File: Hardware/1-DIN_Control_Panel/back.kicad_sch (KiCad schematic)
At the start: 49 parts, among them J1 Selector Knob Connector, J10 2x05 Molex Micro-Fit 3.0 43045, J13 Mode LEDs, J14 Selector Knob Connector, J15 Rotary Switch 1x7, J16 Mode LEDs, J2 Rotary Switch 1x7, J3 2x05 Molex Micro-Fit 3.0 43045, J4 UART Expansion, J5 SW - Aux Jump-Start, J6 SW - Battery Bypass, J7 SW - Master Power, J8 Pot/SW - Brightness, K1 FINDER-40.52, U12 LM324DR, U13 12V->5V Variable Boost Buck C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, U15 LTV-847S, U16 LTV-847S, U5 MMPQ3904, U6 MMPQ3904

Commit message: Fixed BJT math
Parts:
- removed J14: Selector Knob Connector, Connector_Molex:Molex_Micro-Fit_3.0_43045-0812_2x04_P3.00mm_Vertical, symbol Connector_Generic:Conn_01x08
- removed J15: Rotary Switch 1x7, Connector_Molex:Molex_Micro-Fit_3.0_43045-0812_2x04_P3.00mm_Vertical, symbol Connector_Generic:Conn_01x08
- removed J16: Mode LEDs, Connector_Molex:Molex_Micro-Fit_3.0_43045-0812_2x04_P3.00mm_Vertical, symbol Connector_Generic:Conn_01x08
- removed R21: 10kΩ, Resistor_SMD:R_0603_1608Metric_Pad0.98x0.95mm_HandSolder, symbol Device:R_US
- removed U15, U16: LTV-847S, Package_DIP:SMDIP-16_W9.53mm, symbol Isolator:LTV-847S
- added R22, R23, R24, R25, R26, R27, R28, R29: 39kΩ, Resistor_SMD:R_0603_1608Metric_Pad0.98x0.95mm_HandSolder, symbol Device:R_US
- renumbered J1 to J14, J2 to J15, J13 to J16, U5 to U15, U6 to U16
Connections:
- net GND: no longer U16.10 (E4)
- net MODE_1: now also R22.2; no longer U15.15 (B1)
- net MODE_12V: now also R29.2; no longer U16.9 (B4)
- net MODE_2: now also R23.2; no longer U15.13 (B2)
- net MODE_3: now also R24.2; no longer U15.11 (B3)
- net MODE_4: now also R25.2; no longer U15.9 (B4)
- net MODE_5: now also R26.2; no longer U16.15 (B1)
- net MODE_6: now also R27.2; no longer U16.13 (B2)
- net MODE_7: now also R28.2; no longer U16.11 (B3)
- net MODE_PWR_DETECT: now also U16.10 (E4)
- net at J16.8 (Pin_8): now also R9.2
- new net: R27.1, U16.13 (B2)
- new net: R24.1, U15.11 (B3)
- new net: R23.1, U15.13 (B2)
- new net: R26.1, U16.15 (B1)
- new net: R25.1, U15.9 (B4)
- new net: R22.1, U15.15 (B1)
- new net: R28.1, U16.11 (B3)
- new net: R29.1, U16.9 (B4)
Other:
- note added: "Using extra BJT as mode selector 12V detect signal...because why not!"
- note added: "Vbe = 0.7V 12V-ib(39kΩ)-Vbe = 0 -> ib = 0.290mA ic = hFE*ib = 70*0.290mA = 20mA"
- note removed: "Using extra optoisolator as mode selector 12V detect signal...because why not!"
- moved on the sheet: J14, J15, J16, U15A, U15B, U15C, U15D, U16A, U16B, U16C, U16D

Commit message: Almost done with routing
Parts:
- renumbered J14 to J1, J16 to J13, J15 to J2, U15 to U5, U16 to U6
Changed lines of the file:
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@@
   (symbol (lib_id "Panel_Parts:MMPQ3904") (at 102.87 152.4 0) (unit 2)
     (in_bom yes) (on_board yes) (dnp no)
-    (property "Reference" "U16" (at 106.68 151.13 0)
+    (property "Reference" "U6" (at 106.68 151.13 0)
       (effects (font (size 1.27 1.27)) (justify left))
     )
@@
       (project "1-DIN_Control_Panel"
         (path "/9d6c5460-8470-44bf-9076-df961456f999/79705e83-d37e-491a-a216-1b060693c97a"
-          (reference "U16") (unit 2)
+          (reference "U6") (unit 2)
         )
       )
@@
   (symbol (lib_id "Connector_Generic:Conn_01x08") (at 130.81 78.74 90) (unit 1)
     (in_bom yes) (on_board yes) (dnp no)
-    (property "Reference" "J16" (at 135.89 74.93 90)
+    (property "Reference" "J13" (at 135.89 74.93 90)
       (effects (font (size 1.27 1.27)) (justify right))
     )
@@
       (project "1-DIN_Control_Panel"
         (path "/9d6c5460-8470-44bf-9076-df961456f999/79705e83-d37e-491a-a216-1b060693c97a"
-          (reference "J16") (unit 1)
+          (reference "J13") (unit 1)
         )
       )
@@
   (symbol (lib_id "Connector_Generic:Conn_01x08") (at 62.23 74.93 270) (mirror x) (unit 1)
     (in_bom yes) (on_board yes) (dnp no)
-    (property "Reference" "J15" (at 73.66 72.39 90)
+    (property "Reference" "J2" (at 73.66 72.39 90)
       (effects (font (size 1.27 1.27)) (justify left))
     )
@@
       (project "1-DIN_Control_Panel"
         (path "/9d6c5460-8470-44bf-9076-df961456f999/79705e83-d37e-491a-a216-1b060693c97a"
-          (reference "J15") (unit 1)
+          (reference "J2") (unit 1)
         )
       )
@@
   (symbol (lib_id "Panel_Parts:MMPQ3904") (at 102.87 118.11 0) (unit 3)
     (in_bom yes) (on_board yes) (dnp no)
-    (property "Reference" "U15" (at 106.68 116.84 0)
+    (property "Reference" "U5" (at 106.68 116.84 0)
       (effects (font (size 1.27 1.27)) (justify left))
     )
@@
       (project "1-DIN_Control_Panel"
         (path "/9d6c5460-8470-44bf-9076-df961456f999/79705e83-d37e-491a-a216-1b060693c97a"
-          (reference "U15") (unit 3)
+          (reference "U5") (unit 3)
         )
       )
@@
   (symbol (lib_id "Connector_Generic:Conn_01x08") (at 30.48 105.41 180) (unit 1)
     (in_bom yes) (on_board yes) (dnp no)
-    (property "Reference" "J14" (at 38.862 105.7715 0)
+    (property "Reference" "J1" (at 25.4 104.14 0)
       (effects (font (size 1.27 1.27)) (justify right))
     )
@@
       (project "1-DIN_Control_Panel"
         (path "/9d6c5460-8470-44bf-9076-df961456f999/79705e83-d37e-491a-a216-1b060693c97a"
-          (reference "J14") (unit 1)
+          (reference "J1") (unit 1)
         )
       )
@@
   (symbol (lib_id "Panel_Parts:MMPQ3904") (at 102.87 129.54 0) (unit 4)
     (in_bom yes) (on_board yes) (dnp no)
-    (property "Reference" "U15" (at 106.68 128.27 0)
+    (property "Reference" "U5" (at 106.68 128.27 0)
       (effects (font (size 1.27 1.27)) (justify left))
     )
@@
       (project "1-DIN_Control_Panel"
         (path "/9d6c5460-8470-44bf-9076-df961456f999/79705e83-d37e-491a-a216-1b060693c97a"
-          (reference "U15") (unit 4)
+          (reference "U5") (unit 4)
         )
       )
@@
   (symbol (lib_id "Panel_Parts:MMPQ3904") (at 102.87 95.25 0) (unit 1)
     (in_bom yes) (on_board yes) (dnp no)
-    (property "Reference" "U15" (at 106.68 93.98 0)
+    (property "Reference" "U5" (at 106.68 93.98 0)
       (effects (font (size 1.27 1.27)) (justify left))
     )
@@
       (project "1-DIN_Control_Panel"
         (path "/9d6c5460-8470-44bf-9076-df961456f999/79705e83-d37e-491a-a216-1b060693c97a"
-          (reference "U15") (unit 1)
+          (reference "U5") (unit 1)
         )
       )
@@
   (symbol (lib_id "Panel_Parts:MMPQ3904") (at 102.87 163.83 0) (unit 3)
     (in_bom yes) (on_board yes) (dnp no)
-    (property "Reference" "U16" (at 106.68 162.56 0)
+    (property "Reference" "U6" (at 106.68 162.56 0)
       (effects (font (size 1.27 1.27)) (justify left))
     )
@@
       (project "1-DIN_Control_Panel"
         (path "/9d6c5460-8470-44bf-9076-df961456f999/79705e83-d37e-491a-a216-1b060693c97a"
-          (reference "U16") (unit 3)
+          (reference "U6") (unit 3)
         )
       )
@@
   (symbol (lib_id "Panel_Parts:MMPQ3904") (at 102.87 106.68 0) (unit 2)
     (in_bom yes) (on_board yes) (dnp no)
-    (property "Reference" "U15" (at 106.68 105.41 0)
+    (property "Reference" "U5" (at 106.68 105.41 0)
       (effects (font (size 1.27 1.27)) (justify left))
     )
@@
       (project "1-DIN_Control_Panel"
         (path "/9d6c5460-8470-44bf-9076-df961456f999/79705e83-d37e-491a-a216-1b060693c97a"
-          (reference "U15") (unit 2)
+          (reference "U5") (unit 2)
         )
       )
@@
   (symbol (lib_id "Panel_Parts:MMPQ3904") (at 102.87 140.97 0) (unit 1)
     (in_bom yes) (on_board yes) (dnp no)
-    (property "Reference" "U16" (at 106.68 139.7 0)
-      (effects (font (size 1.27 1.27)) (justify left))
-    )
-    (property "Value" "MMPQ3904" (at 87.63 158.75 0)
+    (property "Reference" "U6" (at 106.68 139.7 0)
+      (effects (font (size 1.27 1.27)) (justify left))
+    )
+    (property "Value" "MMPQ3904" (at 87.63 134.62 0)
       (effects (font (size 1.27 1.27)) (justify left))
     )
@@
       (project "1-DIN_Control_Panel"
         (path "/9d6c5460-8470-44bf-9076-df961456f999/79705e83-d37e-491a-a216-1b060693c97a"
-          (reference "U16") (unit 1)
+          (reference "U6") (unit 1)
         )
       )
@@
   (symbol (lib_id "Panel_Parts:MMPQ3904") (at 102.87 175.26 0) (unit 4)
     (in_bom yes) (on_board yes) (dnp no)
-    (property "Reference" "U16" (at 106.68 173.99 0)
+    (property "Reference" "U6" (at 106.68 173.99 0)
       (effects (font (size 1.27 1.27)) (justify left))
     )
@@
       (project "1-DIN_Control_Panel"
         (path "/9d6c5460-8470-44bf-9076-df961456f999/79705e83-d37e-491a-a216-1b060693c97a"
-          (reference "U16") (unit 4)
-        )
-      )
+          (reference "U6") (unit 4)
+        )
+      )

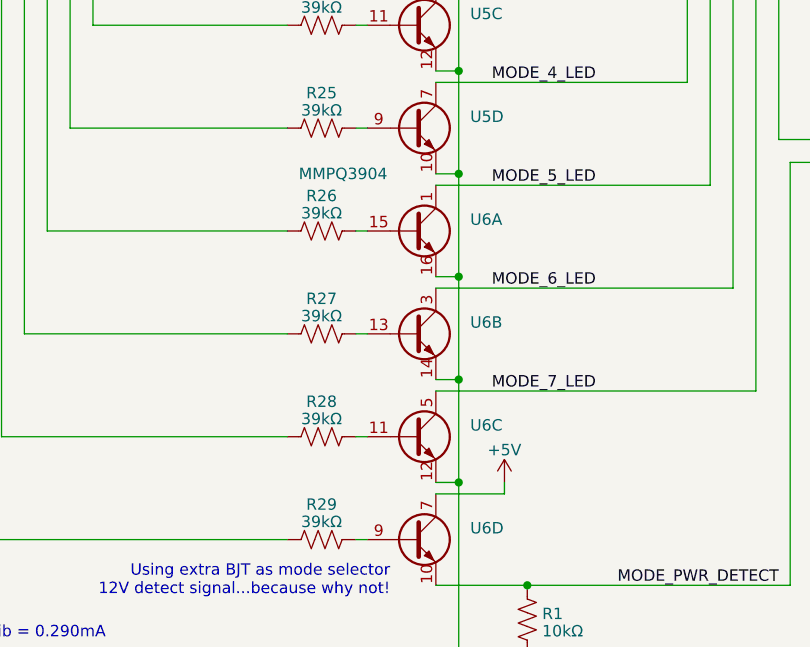
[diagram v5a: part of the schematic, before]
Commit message: Finished routing
Now just need to combine the boards with mousebites
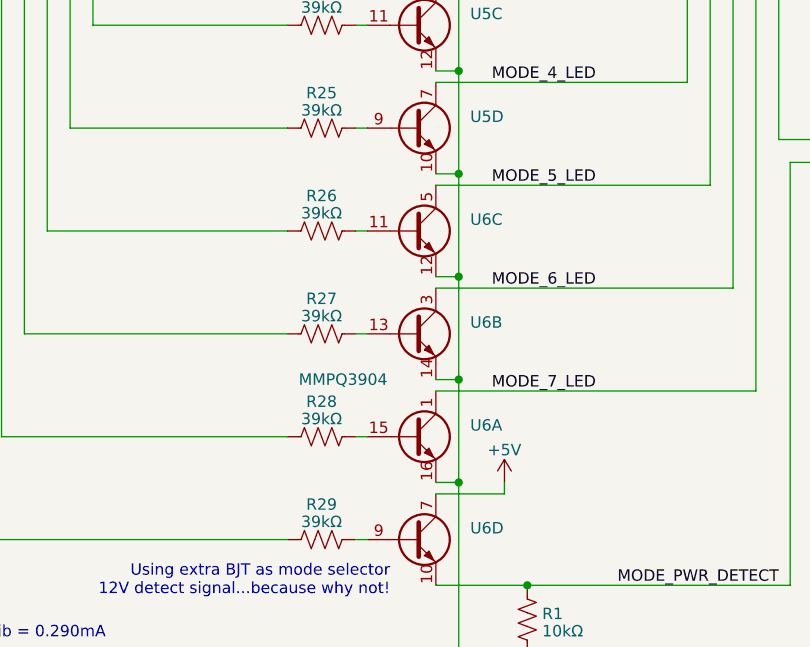
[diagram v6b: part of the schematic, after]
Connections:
- net MODE_5_LED: now also U6.5 (C4), U6.6 (C3); no longer U6.1 (C1), U6.2 (C1)
- net MODE_7_LED: now also U6.1 (C1), U6.2 (C1); no longer U6.5 (C4), U6.6 (C3)
- net at R26.1: now also U6.11 (B3); no longer U6.15 (B1)
- net at R28.1: now also U6.15 (B1); no longer U6.11 (B3)
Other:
- moved on the sheet: U6A, U6C
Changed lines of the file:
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@@
     )
   )
-  (symbol (lib_id "Panel_Parts:MMPQ3904") (at 102.87 163.83 0) (unit 3)
-    (in_bom yes) (on_board yes) (dnp no)
-    (property "Reference" "U6" (at 106.68 162.56 0)
-      (effects (font (size 1.27 1.27)) (justify left))
-    )
-    (property "Value" "MMPQ3904" (at 105.1814 165.1073 0)
+  (symbol (lib_id "Panel_Parts:MMPQ3904") (at 102.87 140.97 0) (unit 3)
+    (in_bom yes) (on_board yes) (dnp no)
+    (property "Reference" "U6" (at 106.68 139.7 0)
+      (effects (font (size 1.27 1.27)) (justify left))
+    )
+    (property "Value" "MMPQ3904" (at 105.1814 142.2473 0)
       (effects (font (size 1.27 1.27)) (justify left) hide)
     )
-    (property "Footprint" "Package_SO:SOIC-16_4.55x10.3mm_P1.27mm" (at 102.87 163.83 0)
-      (effects (font (size 1.27 1.27)) hide)
-    )
-    (property "Datasheet" "https://www.onsemi.com/pdf/datasheet/ffb3904-d.pdf" (at 102.87 163.83 0)
+    (property "Footprint" "Package_SO:SOIC-16_4.55x10.3mm_P1.27mm" (at 102.87 140.97 0)
+      (effects (font (size 1.27 1.27)) hide)
+    )
+    (property "Datasheet" "https://www.onsemi.com/pdf/datasheet/ffb3904-d.pdf" (at 102.87 140.97 0)
       (effects (font (size 1.27 1.27)) hide)
     )
@@
     )
   )
-  (symbol (lib_id "Panel_Parts:MMPQ3904") (at 102.87 140.97 0) (unit 1)
-    (in_bom yes) (on_board yes) (dnp no)
-    (property "Reference" "U6" (at 106.68 139.7 0)
-      (effects (font (size 1.27 1.27)) (justify left))
-    )
-    (property "Value" "MMPQ3904" (at 87.63 134.62 0)
-      (effects (font (size 1.27 1.27)) (justify left))
-    )
-    (property "Footprint" "Package_SO:SOIC-16_4.55x10.3mm_P1.27mm" (at 102.87 140.97 0)
-      (effects (font (size 1.27 1.27)) hide)
-    )
-    (property "Datasheet" "https://www.onsemi.com/pdf/datasheet/ffb3904-d.pdf" (at 102.87 140.97 0)
-      (effects (font (size 1.27 1.27)) hide)
-    )
+  (symbol (lib_id "Panel_Parts:MMPQ3904") (at 102.87 163.83 0) (unit 1)
+    (in_bom yes) (on_board yes) (dnp no)
+    (property "Reference" "U6" (at 106.68 162.56 0)
+      (effects (font (size 1.27 1.27)) (justify left))
+    )
+    (property "Value" "MMPQ3904" (at 87.63 157.48 0)
+      (effects (font (size 1.27 1.27)) (justify left))
+    )
+    (property "Footprint" "Package_SO:SOIC-16_4.55x10.3mm_P1.27mm" (at 102.87 163.83 0)
+      (effects (font (size 1.27 1.27)) hide)
+    )
+    (property "Datasheet" "https://www.onsemi.com/pdf/datasheet/ffb3904-d.pdf" (at 102.87 163.83 0)
+      (effects (font (size 1.27 1.27)) hide)
+    )

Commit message: More tweaks and silkscreen labels
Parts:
- added D11: LED_Filled, LED_THT:LED_D3.0mm, symbol Device:LED_Filled
- added R21: 39kΩ, Resistor_SMD:R_0603_1608Metric_Pad0.98x0.95mm_HandSolder, symbol Device:R_US
- added R30: 150Ω, Resistor_SMD:R_0603_1608Metric_Pad0.98x0.95mm_HandSolder, symbol Device:R_US
- added SW1: SW_SPST, symbol Switch:SW_SPST
- added U14: MMPQ3904, Package_SO:SOIC-16_4.55x10.3mm_P1.27mm, symbol Panel_Parts:MMPQ3904
- added U15: PIC18LF1220-SO, Package_SO:SOIC-18W_7.5x11.6mm_P1.27mm, symbol MCU_Microchip_PIC18:PIC18LF1220-SO
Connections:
- net GND renamed +12V
- net +12V: now also SW1.1 (A), U14.16 (E1)
- new net: R30.1, U14.1 (C1), U14.2 (C1)
- new net: R21.1, U14.15 (B1)
- new net: D11.1 (K), R30.2
- new net: D11.2 (A), U15.6 (RA2/AN2/Vref-)
- new net: R21.2, SW1.2 (B)
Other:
- note added: "+5V PWM"
